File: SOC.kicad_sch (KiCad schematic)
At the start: 64 parts, among them J3 TF01-A, P1 HRO-TYPE-C-31-M-12, P2 WF24HTLAJDNN0#, Q1 Q_NMOS_DSG, SW2 TS-1157-X-A, SW3 TS-1157-X-A, SW4 TS-1157-X-A, SW5 TS-1157-X-A, SW6 TS-1157-X-A, SW7 KLS7-TS3606, SW8 KLS7-TS3606, U12 W25Q128JVSIQ, U4 F1C200S, U8 USBLC6-2SC6, Y1 24M

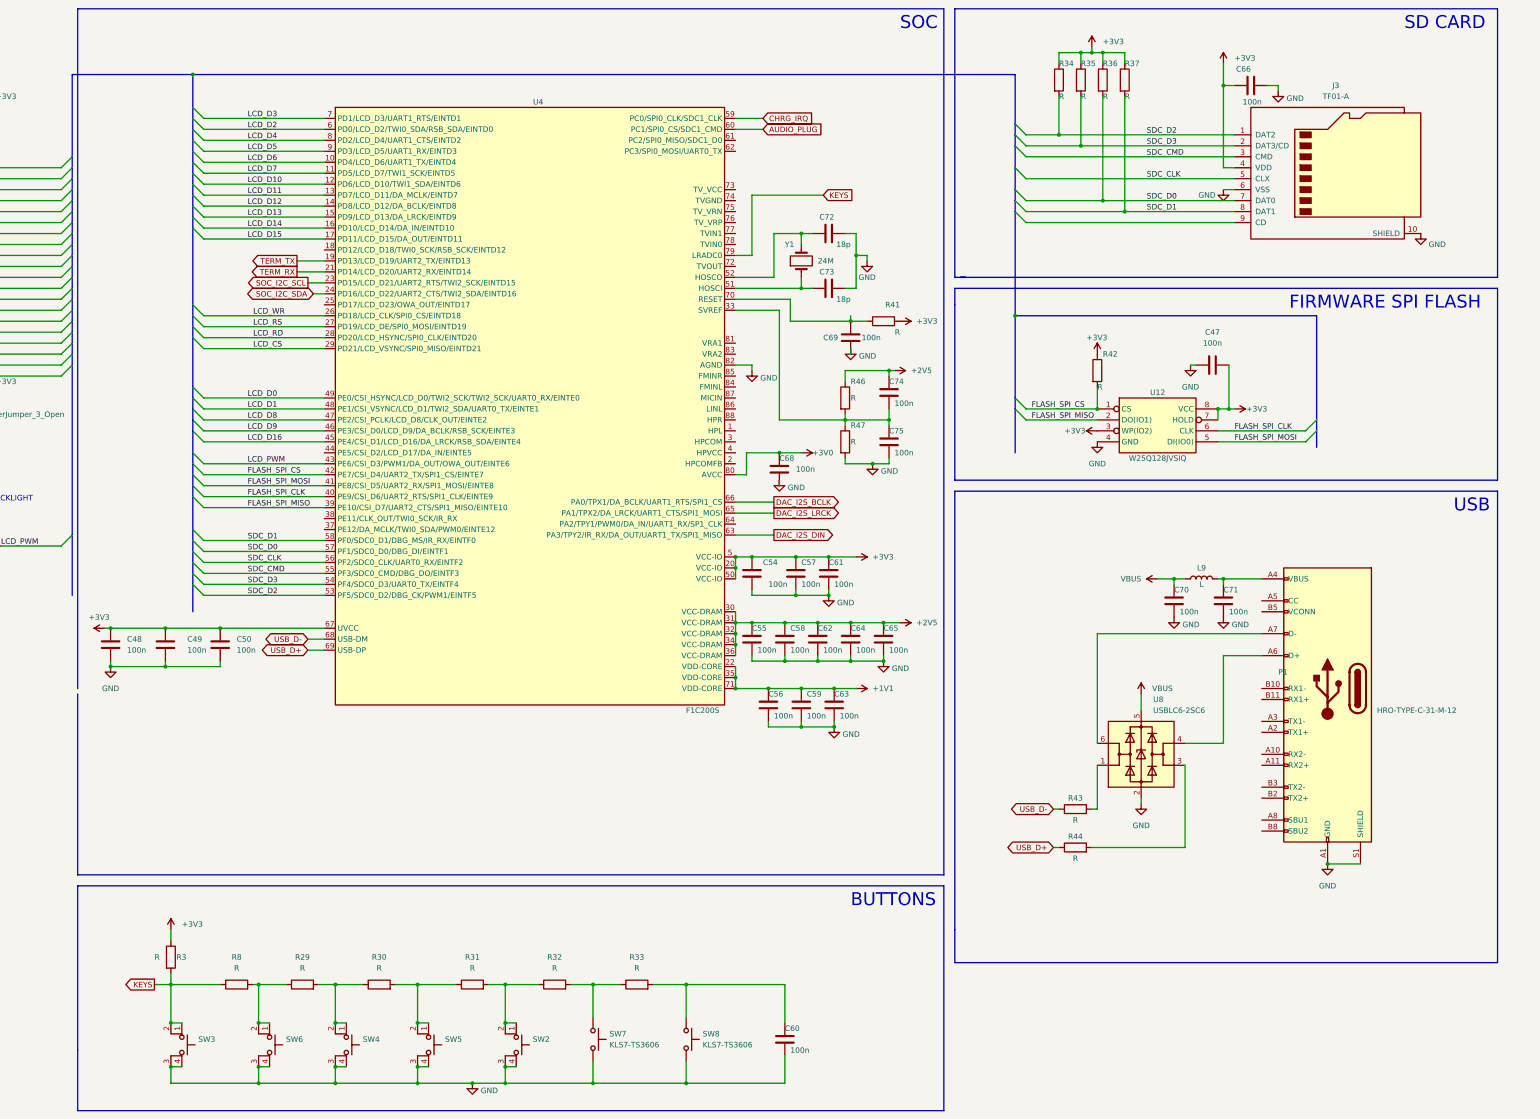
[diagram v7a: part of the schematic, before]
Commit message: added buttons
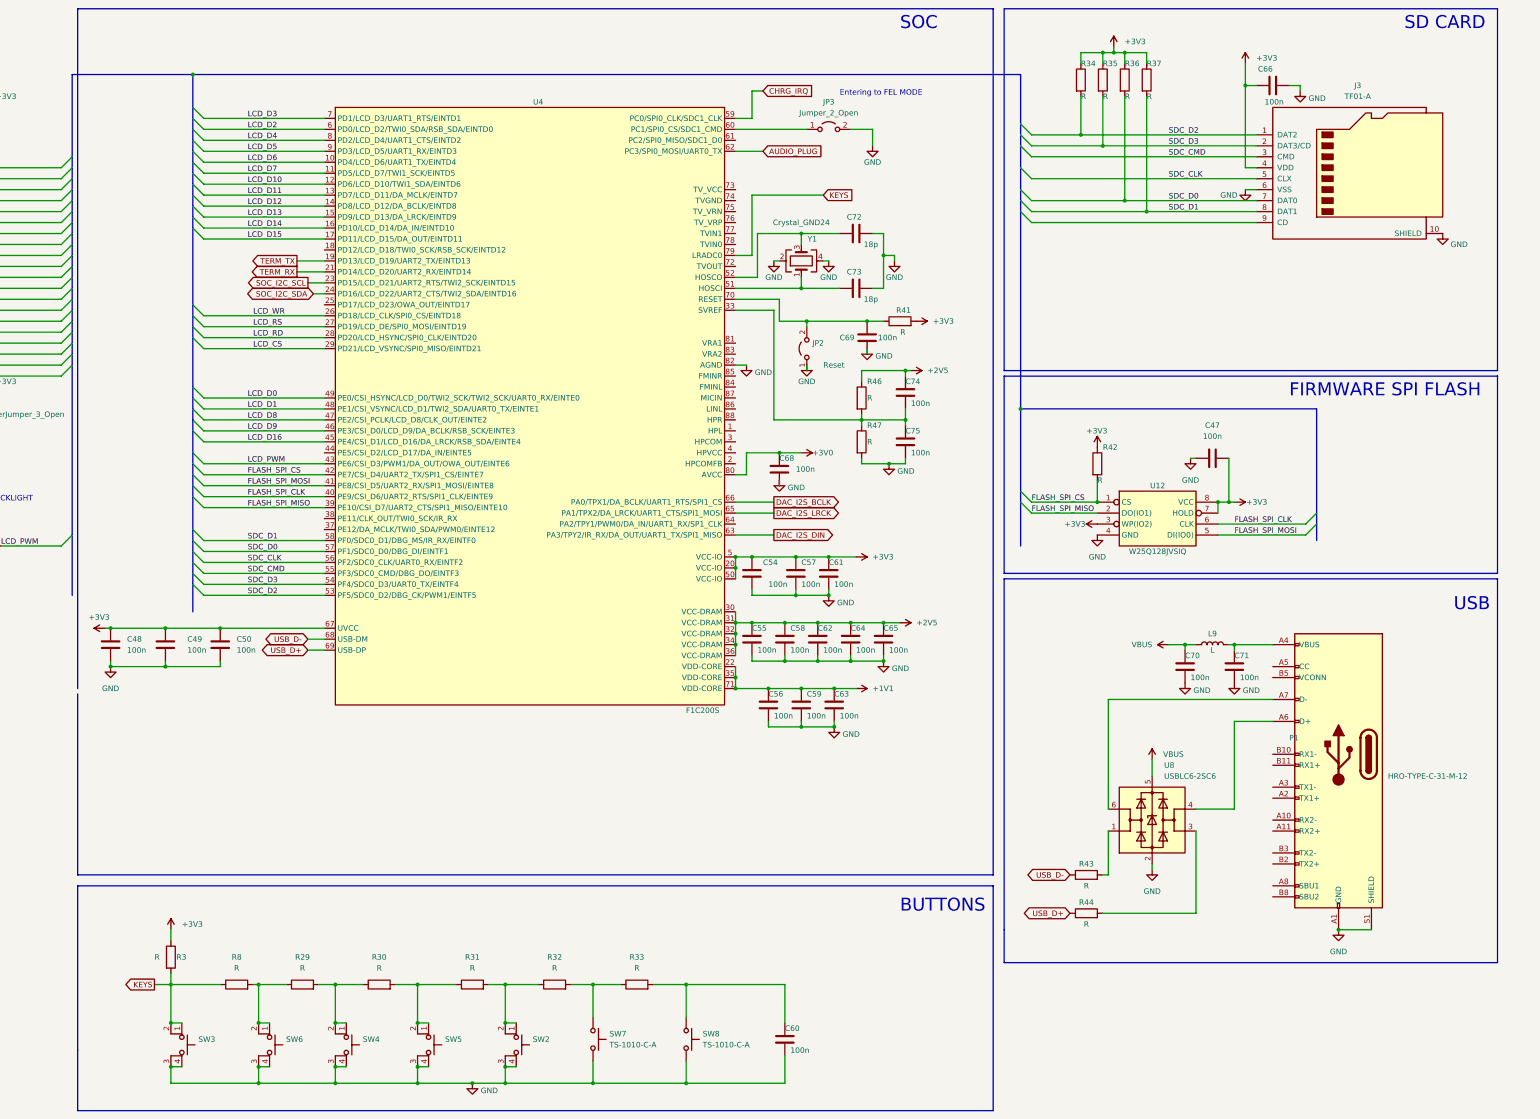
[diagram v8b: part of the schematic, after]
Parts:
- removed Y1: 24M, symbol Device:Crystal
- added JP2: Reset, Jumper:SolderJumper-2_P1.3mm_Open_RoundedPad1.0x1.5mm, symbol Jumper:Jumper_2_Open
- added JP3: Jumper_2_Open, Jumper:SolderJumper-2_P1.3mm_Open_RoundedPad1.0x1.5mm, symbol Jumper:Jumper_2_Open
- added Y1: Crystal_GND24, rlib_crystals:Crystal_SMD_Abracon_ABM8G-4Pin_3.2x2.5mm, symbol rlib_crystal:Crystal_GND24
- SW2, SW3, SW4, SW5, SW6: footprint rclib_buttons:TS-1157-X-A -> rlib_buttons:TS-1157-X-A
- SW7, SW8: value KLS7-TS3606 -> TS-1010-C-A
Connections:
- net AUDIO_PLUG: now also U4.62 (PC3/SPI0_MOSI/UART0_TX); no longer U4.60 (PC1/SPI0_CS/SDC1_CMD)
- net GND: now also JP2.1 (A), JP3.2 (B), Y1.2, Y1.4
- net at C73.1, U4.51 (HOSCI): now also Y1.1
- net at C69.1, R41.1, U4.70 (RESET): now also JP2.2 (B)
- net at C72.1, U4.52 (HOSCO): now also Y1.3
- new net: JP3.1 (A), U4.60 (PC1/SPI0_CS/SDC1_CMD)
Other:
- note added: "Entering to FEL MODE"
- moved on the sheet: C47, C66, C69, C70, C71, C72, C73, C74, C75, J3, L9, P1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
